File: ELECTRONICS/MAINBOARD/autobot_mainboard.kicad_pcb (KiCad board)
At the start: 4 copper layers, 62 x 42.5 mm, 161 parts, among them IC1 DW3210, J1 USB_C_Receptacle_USB2.0_16P, J10 Conn_01x05_Socket, J12 Conn_01x02_Pin, J14 Conn_01x05_Pin, J16 Conn_01x05_Pin, J17 Conn_01x02_Pin, J18 Conn_01x02_Pin, J19 Conn_02x05_Odd_Even, J20 Conn_02x05_Odd_Even, J7 Conn_01x03_Pin, J8 Conn_Coaxial, J9 Conn_Coaxial, Q1 DMG1012T, Q2 DMG1012T, Q3 DMG1012T, SW1 RESET, SW2 BOOT, U1 TVS1400DRV, U10 VL53L1X, U11 VL53L1X, U12 VL53L1X, U13 BMI270, U14 BMI270, U15 TPD4E05U06DQA, U16 LP5907MFX-3.3, U17 STM32G031C6Tx, U18 LP5907MFX-3.3, U19 STM32H743VITx, U2 LMR51430XDDCR, U22 TPD4E05U06DQA, U23 LP5907MFX-3.3, U3 LP5907MFX-3.3, U4 TPD2EUSB30A, U9 VL53L1X, Y1 TXC 8Y38472012, Y2 25mhz placeholder

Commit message: driver board schematic
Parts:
- removed C81: 22u, Capacitor_SMD:C_0402_1005Metric
- removed C81: 22u, Capacitor_SMD:C_0805_2012Metric
- removed C84: 1u, Capacitor_SMD:C_0402_1005Metric
- removed C89, C90, C91, C92, C93, C94: C, Capacitor_SMD:C_0402_1005Metric
- removed R26, R27: 10k, Capacitor_SMD:C_0402_1005Metric
- removed R28, R48: r, Capacitor_SMD:C_0402_1005Metric
- removed R29, R30, R31, R32, R33, R34, R35, R36, R37, R38, R39, R40, R41, R42, R43, R44, R45, R46: 4.7k, Capacitor_SMD:C_0402_1005Metric
- added C10: 1u, Capacitor_SMD:C_0402_1005Metric, F.Cu at (49.6, 33.2)
- added C11: 1u, Capacitor_SMD:C_0402_1005Metric, F.Cu at (52.7, 40.5)
- added C12: 1u, Capacitor_SMD:C_0402_1005Metric, F.Cu at (46.3, 41.0)
- added C13: C, Capacitor_SMD:C_0402_1005Metric, F.Cu at (47.8, 41.0)
- added C14: 47n, Capacitor_SMD:C_0402_1005Metric, F.Cu at (50.2, 41.0)
- added C15: 100u, Capacitor_SMD:C_0402_1005Metric, F.Cu at (14.7, -2.46)
- added C16: 100n, Capacitor_SMD:C_0402_1005Metric, F.Cu at (14.7, -0.49)
- added C17: 100n, Capacitor_SMD:C_0402_1005Metric, F.Cu at (14.7, 1.48)
- added C18: 1u, Capacitor_SMD:C_0402_1005Metric, F.Cu at (14.7, 3.44)
- added C7: 100n, Capacitor_SMD:C_0402_1005Metric, F.Cu at (52.7, 43.5)
- added C74: 1u, Capacitor_SMD:C_0402_1005Metric, F.Cu at (14.7, 5.42)
- added C76: 47n, Capacitor_SMD:C_0402_1005Metric, F.Cu at (14.7, 9.36)
- added C77: C, Capacitor_SMD:C_0402_1005Metric, F.Cu at (14.7, 11.3)
- added C8: 100u, Capacitor_SMD:C_0402_1005Metric, F.Cu at (52.7, 42.5)
- added C9: 100n, Capacitor_SMD:C_0402_1005Metric, F.Cu at (52.7, 41.5)
- added R10: 10K, Resistor_SMD:R_0402_1005Metric, F.Cu at (48.4, 31.1)
- added R11: 22, Resistor_SMD:R_0402_1005Metric, F.Cu at (49.1, 41.0)
- added R12: 10K, Resistor_SMD:R_0402_1005Metric, F.Cu at (17.6, -2.46)
- added R13: 10K, Resistor_SMD:R_0402_1005Metric, F.Cu at (17.6, -0.47)
- added R14: 10K, Resistor_SMD:R_0402_1005Metric, F.Cu at (17.6, 1.52)
- added R23: 10K, Resistor_SMD:R_0402_1005Metric, F.Cu at (17.6, 3.52)
- added R24: 22, Resistor_SMD:R_0402_1005Metric, F.Cu at (17.6, 5.50)
- added R7: 10K, Resistor_SMD:R_0402_1005Metric, F.Cu at (46.3, 31.1)
- added R8: 10K, Resistor_SMD:R_0402_1005Metric, F.Cu at (47.4, 31.1)
- added R9: 10K, Resistor_SMD:R_0402_1005Metric, F.Cu at (44.8, 40.0)
- C75: value 22u -> 1u
- moved FB4 107.6 mm to (30.3, 16.5)
- moved C86 104.1 mm to (30.2, 18.4)
- moved C87 104.1 mm to (30.2, 20.4)
- moved FB1 102.3 mm to (25.4, 16.5)
- moved C31 98.8 mm to (25.3, 18.4)
- moved C32 98.8 mm to (25.3, 20.4)
- moved U22 95.8 mm to (35.4, 11.1)
- moved U15 88.1 mm to (35.2, 17.7)
- moved C95 82.6 mm to (30.5, 9.84)
- moved C96 82.6 mm to (30.5, 11.8)
- moved U23 82.6 mm to (26.5, 11.2)
- moved C75 68.5 mm to (14.7, 7.38)
- moved C36 47.6 mm to (35.2, 22.7)
- moved C37 44.4 mm to (37.0, 30.9), turned to 180 degrees
- moved J12 36.6 mm to (58.7, 6.29)
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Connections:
- C75 pad 1: VDD -> +24V
- C75 pad 2: GNDREF -> Net-(U6-CP)
- U17 pad 11: unconnected-(U17-PA0-Pad11) -> /AMT102_L/AMT_A
- U17 pad 12: unconnected-(U17-PA1-Pad12) -> /AMT102_L/AMT_B
- U17 pad 13: unconnected-(U17-PA2-Pad13) -> /AMT102_L/AMT_X
- U17 pad 16: unconnected-(U17-PA5-Pad16) -> /STM32G0/DACOUT1_R
- U17 pad 17: unconnected-(U17-PA6-Pad17) -> /STM32G0/DACOUT2_R
- U17 pad 18: unconnected-(U17-PA7-Pad18) -> /STM32G0/PWM_R
- U17 pad 19: unconnected-(U17-PB0-Pad19) -> /STM32G0/DIR_R
- U17 pad 20: unconnected-(U17-PB1-Pad20) -> /STM32G0/EXT_WD_R
- U17 pad 21: unconnected-(U17-PB2-Pad21) -> /STM32G0/FG_R
- U17 pad 23: unconnected-(U17-PB11-Pad23) -> /STM32G0/nFAULT_R
- U17 pad 24: unconnected-(U17-PB12-Pad24) -> /STM32G0/DRVOFF_R
- U17 pad 25: unconnected-(U17-PB13-Pad25) -> /STM32G0/BRAKE_R
- U17 pad 28: unconnected-(U17-PA8-Pad28) -> /AMT102_L/AMT_X
- U17 pad 30: unconnected-(U17-PC6-Pad30) -> /AMT102_R/AMT_A
- U17 pad 31: unconnected-(U17-PC7-Pad31) -> /AMT102_R/AMT_B
- U17 pad 38: unconnected-(U17-PD0-Pad38) -> /STM32G0/EXT_WD
- U17 pad 39: unconnected-(U17-PD1-Pad39) -> /STM32G0/BRAKE
- U17 pad 40: unconnected-(U17-PD2-Pad40) -> /STM32G0/DACOUT2
- U17 pad 41: unconnected-(U17-PD3-Pad41) -> /STM32G0/DACOUT1
- U17 pad 42: unconnected-(U17-PB3-Pad42) -> /STM32G0/nFAULT
- U17 pad 43: unconnected-(U17-PB4-Pad43) -> /STM32G0/DRVOFF
- U17 pad 44: unconnected-(U17-PB5-Pad44) -> /STM32G0/DIR
- U17 pad 45: unconnected-(U17-PB6-Pad45) -> /STM32G0/PWM
- U17 pad 46: unconnected-(U17-PB7-Pad46) -> /STM32G0/FG
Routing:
- net VDD: track 11.8 -> 0.00 mm
- net (no net): track 0.00 -> 11.8 mm
- net Net-(U5-GND_BK): track 0.00 -> 0.60 mm
- added copper zone on In2.Cu, net (none)
- removed copper zone on In2.Cu, net VDD
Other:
- board size 62 x 42.5 mm -> 50 x 35.5 mm

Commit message: 10/3 final
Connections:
- U17 pad 15: unconnected-(U17-PA4-Pad15) -> /STM32G0/PWM_R
- U17 pad 16: /STM32G0/DACOUT1_R -> /STM32G0/DACOUT2_R
- U17 pad 17: /STM32G0/DACOUT2_R -> /STM32G0/DACOUT1_R
- U17 pad 18: /STM32G0/PWM_R -> /STM32G0/BRAKE_R
- U17 pad 21: /STM32G0/FG_R -> unconnected-(U17-PB2-Pad21)
- U17 pad 22: /STM32G0/SCL_R -> unconnected-(U17-PB10-Pad22)
- U17 pad 25: /STM32G0/BRAKE_R -> /STM32G0/SCL_R
- U17 pad 27: unconnected-(U17-PB15-Pad27) -> /STM32G0/FG_R
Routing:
- net /STM32G0/FG_R: track 0.00 -> 14.1 mm
- net /STM32G0/PWM_R: track 0.00 -> 14.0 mm
- net /STM32G0/SDA_R: track 0.00 -> 12.6 mm
- net /STM32G0/SCL_R: track 0.00 -> 11.1 mm
- net /STM32G0/EXT_WD_R: track 0.00 -> 6.51 mm
- net /STM32G0/DIR_R: track 0.00 -> 5.39 mm
- net /STM32G0/BRAKE_R: track 0.00 -> 5.39 mm
- net /STM32G0/DACOUT2_R: track 0.00 -> 5.18 mm
- net /STM32G0/DACOUT1_R: track 0.00 -> 5.18 mm
- net /STM32G0/nFAULT_R: track 0.00 -> 2.31 mm

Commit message: almost done
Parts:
- removed J14, J16: Conn_01x05_Pin, Connector_JST:JST_PH_B5B-PH-K_1x05_P2.00mm_Vertical
- removed the J17 at (52.1, 6.29)
- removed the J17 at (-30.9, 47.6)
- removed U15, U22: TPD4E05U06DQA, Package_SON:USON-10_2.5x1.0mm_P0.5mm
- removed U17: STM32G031C6Tx, Package_QFP:LQFP-48_7x7mm_P0.5mm
- added D10: D_TVS, Diode_SMD:D_0402_1005Metric, F.Cu at (19.1, 52.8)
- added D11: D_TVS, Diode_SMD:D_0603_1608Metric, F.Cu at (24.5, 45.5)
- added D12: D_TVS, Diode_SMD:D_0603_1608Metric, F.Cu at (50.0, 28.4)
- added D5: D_TVS, Diode_SMD:D_0402_1005Metric, F.Cu at (54.4, 25.8)
- added D6: D_TVS, Diode_SMD:D_0402_1005Metric, F.Cu at (19.1, 48.8)
- added D7: D_TVS, Diode_SMD:D_0402_1005Metric, F.Cu at (54.4, 23.8)
- added D8: D_TVS, Diode_SMD:D_0402_1005Metric, F.Cu at (19.1, 50.8)
- added D9: D_TVS, Diode_SMD:D_0402_1005Metric, F.Cu at (54.4, 21.8)
- added J17: Conn_01x02_Pin, Connector_JST:JST_PH_B2B-PH-K_1x02_P2.00mm_Vertical, F.Cu at (56.6, 54.2)
- added U7: STM32G031C_4-6-8_Tx, Package_QFP:LQFP-48_7x7mm_P0.5mm, F.Cu at (37.0, 37.0)
- C15, C8: footprint Capacitor_SMD:C_0402_1005Metric -> MyFootprintLibrary:CAP-TH_BD8.0-P3.50-D0.6-FD
- moved J12 266.9 mm to (319.6, 62.3), turned to 90 degrees
- moved J20 207.9 mm to (21.3, 20.3), turned to 90 degrees
- moved C15 63.1 mm to (55.8, 45.5)
- moved R12 52.9 mm to (40.7, 45.2), turned to 90 degrees
- moved R13 50.6 mm to (39.5, 45.2), turned to 90 degrees
- moved R23 46.5 mm to (38.3, 45.2), turned to 90 degrees
- moved C33 44.3 mm to (58.4, 30.3)
- moved C18 38.6 mm to (24.2, 40.8), turned to 180 degrees
- moved C8 37.2 mm to (18.3, 28.5), turned to 180 degrees
- moved C88 36.8 mm to (15.7, 44.3), turned to -90 degrees
- moved J18 35.8 mm to (38.0, 51.9)
- moved R14 34.0 mm to (30.4, 33.0), turned to -90 degrees
- moved C16 33.5 mm to (23.6, 31.9)
- moved C17 32.1 mm to (21.6, 32.9), turned to 180 degrees
- moved C74 31.2 mm to (28.4, 33.5), turned to 180 degrees
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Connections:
- U5 pad 41: (no net) -> GNDREF
- U6 pad 41: (no net) -> GNDREF
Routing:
- net +5V: track 0.00 -> 84.1 mm, vias 0 -> 7
- net /AMT102_L/AMT_X: track 0.00 -> 36.6 mm
- net /AMT102_L/AMT_B: track 0.00 -> 30.9 mm
- net +3V3: track 0.00 -> 30.5 mm, vias 0 -> 4
- net /AMT102_R/AMT_X: track 0.00 -> 29.1 mm, vias 0 -> 2
- net /AMT102_L/AMT_A: track 0.00 -> 28.9 mm
- net /STM32G0/SWCLK: track 0.00 -> 28.7 mm, vias 0 -> 2
- net /AMT102_R/AMT_B: track 0.00 -> 26.2 mm
- net /STM32G0/SWDIO: track 0.00 -> 26.1 mm, vias 0 -> 1
- net GNDREF: track 0.00 -> 24.9 mm, vias 0 -> 14
- net /AMT102_R/AMT_A: track 0.00 -> 24.7 mm
- net /STM32G0/DRVOFF: track 0.00 -> 18.8 mm
- net /STM32G0/SCL_R: track 11.1 -> 26.7 mm, vias 0 -> 2
- net /STM32G0/DRVOFF_R: track 0.00 -> 14.0 mm, vias 0 -> 2
- net /STM32G0/SDA_R: track 12.6 -> 25.6 mm, vias 0 -> 2
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- added copper zone on F.Cu, net +24V
- added copper zone on B.Cu, net +3V3
- added copper zone on F.Cu, net +3V3
- added copper zone on In2.Cu, net +3V3
- added copper zone on B.Cu, net +5V
- added copper zone on F.Cu, net +5V
- removed copper zone on In2.Cu, net (none)
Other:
- board size 50 x 35.5 mm -> 50 x 38.5 mm

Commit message: driver board completed. Prelim, polish later
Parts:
- moved R7 30.6 mm to (45.6, 45.2), turned to 90 degrees
- moved R10 30.5 mm to (42.9, 45.2), turned to 90 degrees
- moved R8 29.7 mm to (44.3, 45.2), turned to 90 degrees
- moved R9 28.9 mm to (47.0, 45.2), turned to 90 degrees
- moved C18 0.06 mm to (24.1, 40.9)
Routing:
- net +3V3: track 30.5 -> 56.2 mm, vias 4 -> 5
- net GNDREF: track 24.9 -> 45.0 mm, vias 14 -> 20
- net /STM32G0/FG: track 9.45 -> 24.5 mm, vias 0 -> 2
- net /STM32G0/SDA: track 8.72 -> 22.9 mm, vias 0 -> 2
- net /STM32G0/SCL: track 8.03 -> 20.4 mm, vias 0 -> 2
- net Net-(J2-Pin_1): track 1.19 -> 7.22 mm
- net Net-(J2-Pin_2): track 1.19 -> 7.16 mm
- net Net-(J2-Pin_3): track 1.19 -> 7.05 mm
- net Net-(J3-Pin_3): track 1.19 -> 6.92 mm
- net Net-(J3-Pin_1): track 1.19 -> 6.92 mm
- net Net-(J3-Pin_2): track 1.19 -> 6.90 mm
- net /STM32G0/nFAULT: track 9.59 -> 13.6 mm
- net /STM32G0/SCL_R: track 26.7 -> 26.2 mm
- net /STM32G0/SWDIO: track 26.1 -> 25.5 mm
- added copper zone on In1.Cu, net GNDREF

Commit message: smth
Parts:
- moved U12 102.1 mm to (267.4, 26.1)
- moved U19 75.8 mm to (273.7, 75.0)
- moved IC1 38.3 mm to (300.3, 75.4)
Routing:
- net /STM32G0/USART_RX: track 4.37 -> 6.51 mm, vias 0 -> 1
- net /STM32G0/USART_TX: track 4.33 -> 5.45 mm, vias 0 -> 1
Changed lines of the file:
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@@
 	(footprint "MyFootprintLibrary:qfn_DW3220_QOR-M"
 		(layer "F.Cu")
-		(at 319.3583 42.1783)
+		(at 300.2981 75.400001)
 		(tags "DW3220 ")
 		(property "Reference" "IC1"
@@
 	(footprint "Connector_JST:JST_PH_S6B-PH-K_1x06_P2.00mm_Horizontal"
 		(layer "F.Cu")
-		(at 358.3 72.53)
+		(at 267.4 26.05)
 		(descr "JST PH series connector, S6B-PH-K (http://www.jst-mfg.com/product/pdf/eng/ePH.pdf)")
 		(tags "connector JST PH horizontal")
@@
 	(footprint "Package_QFP:LQFP-100_14x14mm_P0.5mm"
 		(layer "F.Cu")
-		(at 315.96 12.13)
+		(at 273.7 75)
 		(descr "LQFP, 100 Pin (https://www.nxp.com/docs/en/package-information/SOT407-1.pdf)")
 		(tags "LQFP QFP")
@@
 	)
 	(segment
+		(start 35.6 36.8)
+		(end 35.1 36.8)
+		(width 0.2)
+		(layer "F.Cu")
+		(net "/STM32G0/USART_TX")
+	)
+	(segment
+		(start 36.6 37.8)
+		(end 35.6 36.8)
+		(width 0.2)
+		(layer "F.Cu")
+		(net "/STM32G0/USART_TX")
+	)
+	(segment
 		(start 36.6 39.45)
-		(end 36.6 37)
+		(end 36.6 37.8)
 		(width 0.2)
 		(layer "F.Cu")
@@
 		(net "/STM32G0/USART_TX")
 	)
+	(via
+		(at 35.1 36.8)
+		(size 0.6)
+		(drill 0.3)
+		(layers "F.Cu" "B.Cu")
+		(net "/STM32G0/USART_TX")
+	)
+	(segment
+		(start 37.75 39.85)
+		(end 37.3 39.4)
+		(width 0.2)
+		(layer "F.Cu")
+		(net "/STM32G0/USART_RX")
+	)
+	(segment
+		(start 37.3 37.2)
+		(end 36 35.9)
+		(width 0.2)
+		(layer "F.Cu")
+		(net "/STM32G0/USART_RX")
+	)
 	(segment
 		(start 37.75 41.1875)
@@
 	(segment
 		(start 37.3 39.4)
-		(end 37.3 37)
+		(end 37.3 37.2)
 		(width 0.2)
 		(layer "F.Cu")
@@
 	)
 	(segment
-		(start 37.75 39.85)
-		(end 37.3 39.4)
+		(start 36 35.9)
+		(end 35.5 35.9)
 		(width 0.2)
 		(layer "F.Cu")
 		(net "/STM32G0/USART_RX")
 	)
+	(via
+		(at 35.5 35.9)
+		(size 0.6)
+		(drill 0.3)
+		(layers "F.Cu" "B.Cu")
+		(net "/STM32G0/USART_RX")
+	)

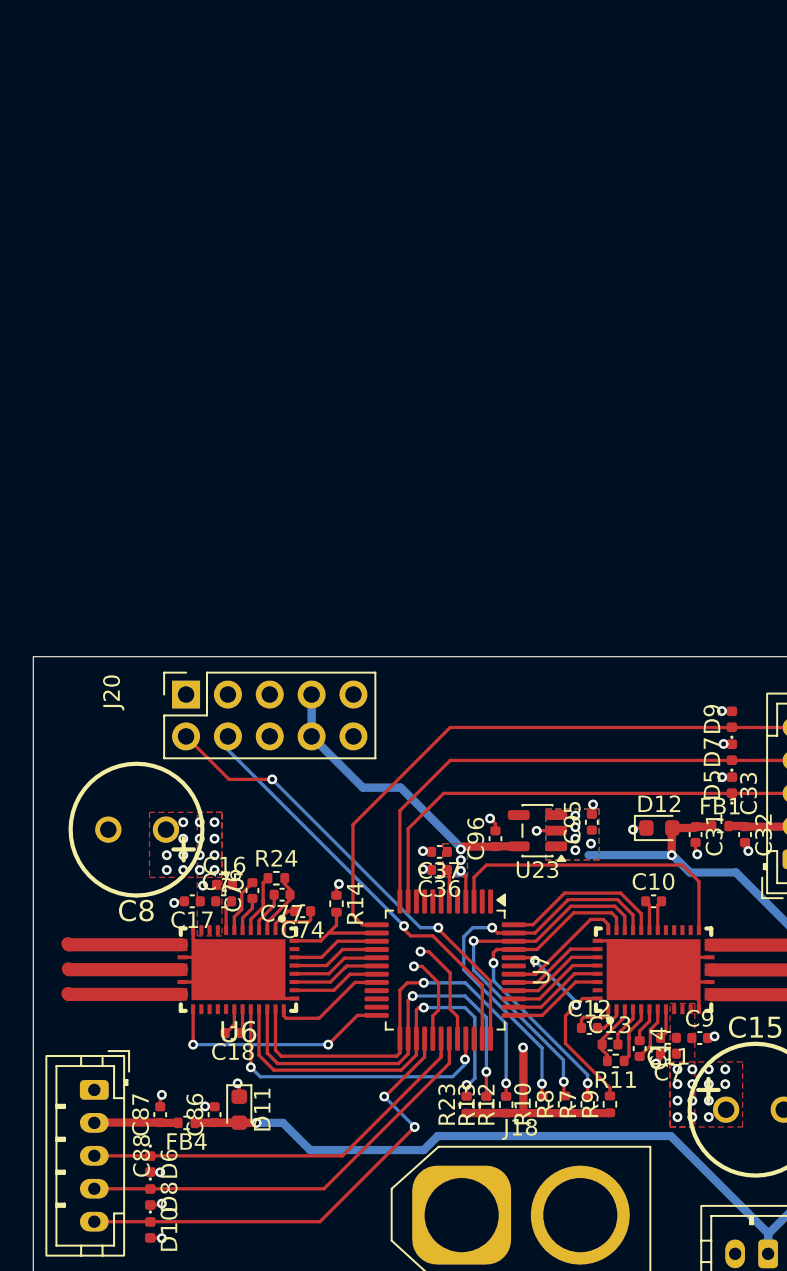
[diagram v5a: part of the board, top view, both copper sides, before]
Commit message: add mosfets
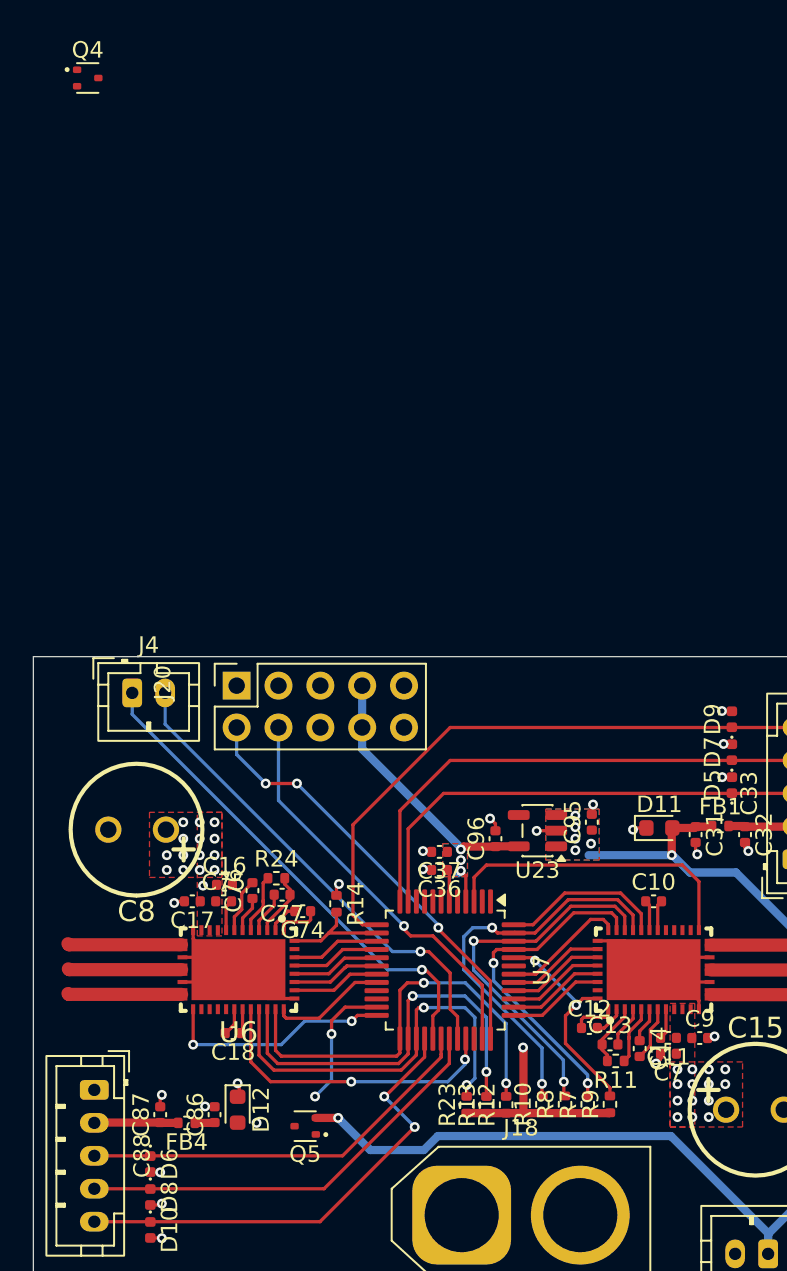
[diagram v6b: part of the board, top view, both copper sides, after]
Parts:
- added J4: Conn_01x02_Socket, Connector_JST:JST_PH_B2B-PH-K_1x02_P2.00mm_Vertical, F.Cu at (18.0, 20.2)
- added Q4: DMG1012T, Package_TO_SOT_SMD:SOT-523, F.Cu at (15.3, -17.1)
- added Q5: DMG1012T, Package_TO_SOT_SMD:SOT-523, F.Cu at (28.5, 46.5)
- moved D12 30.8 mm to (24.4, 45.5), turned to -90 degrees
- moved D11 30.7 mm to (50.0, 28.4), turned to 0 degrees
- moved J20 3.12 mm to (24.3, 19.8)
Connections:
- C31 pad 1: +5V -> Net-(Q4-D)
- C86 pad 1: +5V -> Net-(Q5-D)
- FB1 pad 1: +5V -> Net-(Q4-D)
- FB4 pad 1: +5V -> Net-(Q5-D)
- U7 pad 23: unconnected-(U7-PB11-Pad23) -> /AMT102_R/AMT_GATE
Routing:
- net /STM32G0/USART_TX: track 5.45 -> 30.2 mm
- net /STM32G0/USART_RX: track 6.51 -> 29.6 mm
- net +5V: track 84.1 -> 74.2 mm, vias 7 -> 8
- net /AMT102_R/AMT_GATE: track 0.00 -> 8.09 mm, vias 0 -> 2
- net +3V3: track 56.2 -> 54.1 mm
- net /STM32G0/SWCLK: track 28.2 -> 26.4 mm, vias 2 -> 3
- net Net-(Q5-D): track 0.00 -> 1.20 mm
- net /STM32G0/SWDIO: track 25.5 -> 24.8 mm

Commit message: change tvs
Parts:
- D10, D5, D6, D7, D8, D9: footprint Diode_SMD:D_0402_1005Metric -> Diode_SMD:D_SOD-923
- moved Q4 56.7 mm to (48.5, 28.8), turned to 180 degrees
- moved IC1 24.8 mm to (317.7, 93.1)
- moved D11 1.22 mm to (51.0, 29.1), turned to 90 degrees
- moved D5 0.10 mm to (54.4, 25.9)
- moved D7 0.10 mm to (54.4, 23.9)
- moved D9 0.10 mm to (54.4, 21.9)
- moved D6 0.10 mm to (19.1, 48.7)
- moved D8 0.10 mm to (19.1, 50.7)
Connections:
- C31 pad 1: Net-(Q4-D) -> +5V
- C86 pad 1: Net-(Q5-D) -> +5V
- FB1 pad 1: Net-(Q4-D) -> +5V
- FB4 pad 1: Net-(Q5-D) -> +5V
- Q4 pad 3: Net-(Q4-D) -> +5V
- Q5 pad 3: Net-(Q5-D) -> +5V
- U7 pad 1: unconnected-(U7-PC13-Pad1) -> /AMT102_L/AMT_GATE
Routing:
- net /AMT102_L/AMT_GATE: track 0.00 -> 12.7 mm, vias 0 -> 2
- net +5V: track 74.2 -> 81.4 mm
- net /AMT102_R/AMT_GATE: track 8.09 -> 11.8 mm
- net Net-(Q5-D): track 1.20 -> 0.00 mm
- net GNDREF: track 45.0 -> 45.9 mm

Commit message: add tvs1400 with with ass routing
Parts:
- added U8: TVS1400DRV, Package_SON:WSON-6-1EP_2x2mm_P0.65mm_EP1x1.6mm, F.Cu at (31.6, 53.7)
- moved D10 0.10 mm to (19.1, 52.7)
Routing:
- net +24V: track 0.00 -> 7.77 mm
- net GNDREF: track 45.9 -> 48.1 mm, vias 20 -> 22
